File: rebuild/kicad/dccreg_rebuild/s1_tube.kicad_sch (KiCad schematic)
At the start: 11 parts

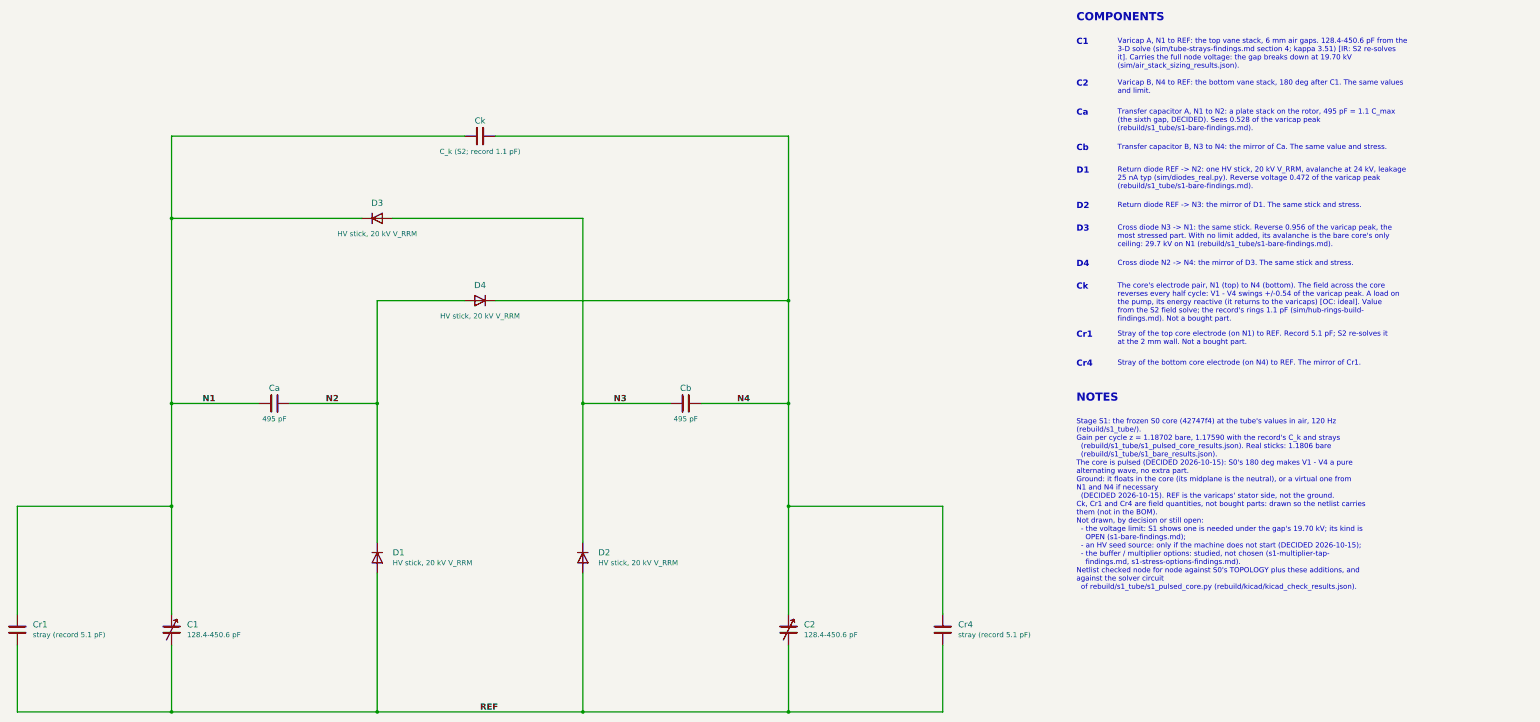
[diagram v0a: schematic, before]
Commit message: feat(rebuild): one KiCad project with a sheet per stage
The designer asked for all stages and changes in one project, each on
its own sheet. rebuild/kicad/dccreg_rebuild/ replaces the two separate
projects: a root sheet indexes the stages, with S0 and S1 as sheets 2
and 3. Each stage numbers its parts in its own hundred (S0 1xx, S1 2xx),
and the nets stay local to their sheet. The layout the designer accepted
is unchanged.

The check exports the project netlist, cuts it by sheet and compares each
stage with its source: S0 against TOPOLOGY and s0_base.cir, S1 against
TOPOLOGY plus the additions and the pulsed-core solver. All match, and
the ERC is clean. A new stage is one entry in STAGES.

Co-Authored-By: Claude Opus 5.5 <noreply@anthropic.com>
Claude-Session: https://claude.ai/code/session_01EZwGpTFL1hyaEya41kJtBw
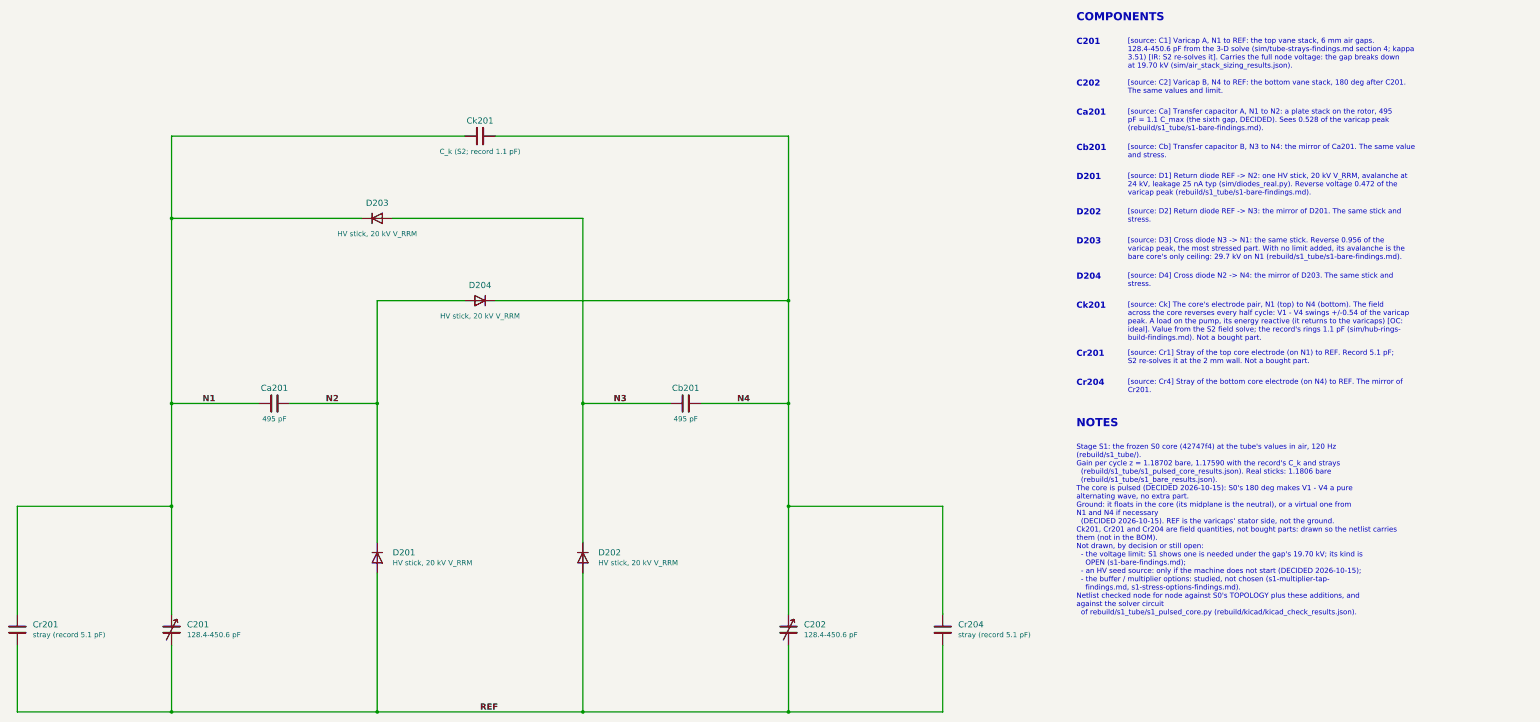
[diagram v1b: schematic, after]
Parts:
- renumbered C1 to C201, C2 to C202, Ca to Ca201, Cb to Cb201, Ck to Ck201, Cr1 to Cr201, Cr4 to Cr204, D1 to D201, D2 to D202, D3 to D203, D4 to D204
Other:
- note added: "C201"
- note added: "C202"
- note added: "Ca201"
- note added: "Cb201"
- note added: "Ck201"
- note added: "Cr201"
- note added: "Cr204"
- note added: "D201"
- note added: "D202"
- note added: "D203"
- note added: "D204"
- note added: "[source: C1] Varicap A, N1 to REF: the top vane stack, 6 mm air gaps. 128.4-450.6 pF from the 3-D solve (sim/tube-strays-findings.md section 4; kappa 3.51) [IR: S2 re-solves it]. Carries the full node voltage: the gap breaks down at 19.70 kV (sim/air_stack_sizing_results.json)."
- note added: "[source: C2] Varicap B, N4 to REF: the bottom vane stack, 180 deg after C201. The same values and limit."
- note added: "[source: Ca] Transfer capacitor A, N1 to N2: a plate stack on the rotor, 495 pF = 1.1 C_max (the sixth gap, DECIDED). Sees 0.528 of the varicap peak (rebuild/s1_tube/s1-bare-findings.md)."
- note added: "[source: Cb] Transfer capacitor B, N3 to N4: the mirror of Ca201. The same value and stress."
- note added: "[source: Ck] The core's electrode pair, N1 (top) to N4 (bottom). The field across the core reverses every half cycle: V1 - V4 swings +/-0.54 of the varicap peak. A load on the pump, its energy reactive (it returns to the varicaps) [OC: ideal]. Value from the S2 field solve; the record's rings 1.1 pF (sim/hub-rings- build-findings.md). Not a bought part."
- note added: "[source: Cr1] Stray of the top core electrode (on N1) to REF. Record 5.1 pF; S2 re-solves it at the 2 mm wall. Not a bought part."
- note added: "[source: Cr4] Stray of the bottom core electrode (on N4) to REF. The mirror of Cr201."
- note added: "[source: D1] Return diode REF -> N2: one HV stick, 20 kV V_RRM, avalanche at 24 kV, leakage 25 nA typ (sim/diodes_real.py). Reverse voltage 0.472 of the varicap peak (rebuild/s1_tube/s1-bare-findings.md)."
- note added: "[source: D2] Return diode REF -> N3: the mirror of D201. The same stick and stress."
- note added: "[source: D3] Cross diode N3 -> N1: the same stick. Reverse 0.956 of the varicap peak, the most stressed part. With no limit added, its avalanche is the bare core's only ceiling: 29.7 kV on N1 (rebuild/s1_tube/s1-bare-findings.md)."
- note added: "[source: D4] Cross diode N2 -> N4: the mirror of D203. The same stick and stress."
- note removed: "C1"
- note removed: "C2"
- note removed: "Ca"
- note removed: "Cb"
- note removed: "Ck"
- note removed: "Cr1"
- note removed: "Cr4"
- note removed: "Cross diode N2 -> N4: the mirror of D3. The same stick and stress."
- note removed: "Cross diode N3 -> N1: the same stick. Reverse 0.956 of the varicap peak, the most stressed part. With no limit added, its avalanche is the bare core's only ceiling: 29.7 kV on N1 (rebuild/s1_tube/s1-bare-findings.md)."
- note removed: "D1"
- note removed: "D2"
- note removed: "D3"
- note removed: "D4"
- note removed: "Return diode REF -> N2: one HV stick, 20 kV V_RRM, avalanche at 24 kV, leakage 25 nA typ (sim/diodes_real.py). Reverse voltage 0.472 of the varicap peak (rebuild/s1_tube/s1-bare-findings.md)."
- note removed: "Return diode REF -> N3: the mirror of D1. The same stick and stress."
- note removed: "Stray of the bottom core electrode (on N4) to REF. The mirror of Cr1."
- note removed: "Stray of the top core electrode (on N1) to REF. Record 5.1 pF; S2 re-solves it at the 2 mm wall. Not a bought part."
- note removed: "The core's electrode pair, N1 (top) to N4 (bottom). The field across the core reverses every half cycle: V1 - V4 swings +/-0.54 of the varicap peak. A load on the pump, its energy reactive (it returns to the varicaps) [OC: ideal]. Value from the S2 field solve; the record's rings 1.1 pF (sim/hub-rings-build- findings.md). Not a bought part."
- note removed: "Transfer capacitor A, N1 to N2: a plate stack on the rotor, 495 pF = 1.1 C_max (the sixth gap, DECIDED). Sees 0.528 of the varicap peak (rebuild/s1_tube/s1-bare-findings.md)."
- note removed: "Transfer capacitor B, N3 to N4: the mirror of Ca. The same value and stress."
- note removed: "Varicap A, N1 to REF: the top vane stack, 6 mm air gaps. 128.4-450.6 pF from the 3-D solve (sim/tube-strays-findings.md section 4; kappa 3.51) [IR: S2 re-solves it]. Carries the full node voltage: the gap breaks down at 19.70 kV (sim/air_stack_sizing_results.json)."
- note removed: "Varicap B, N4 to REF: the bottom vane stack, 180 deg after C1. The same values and limit."

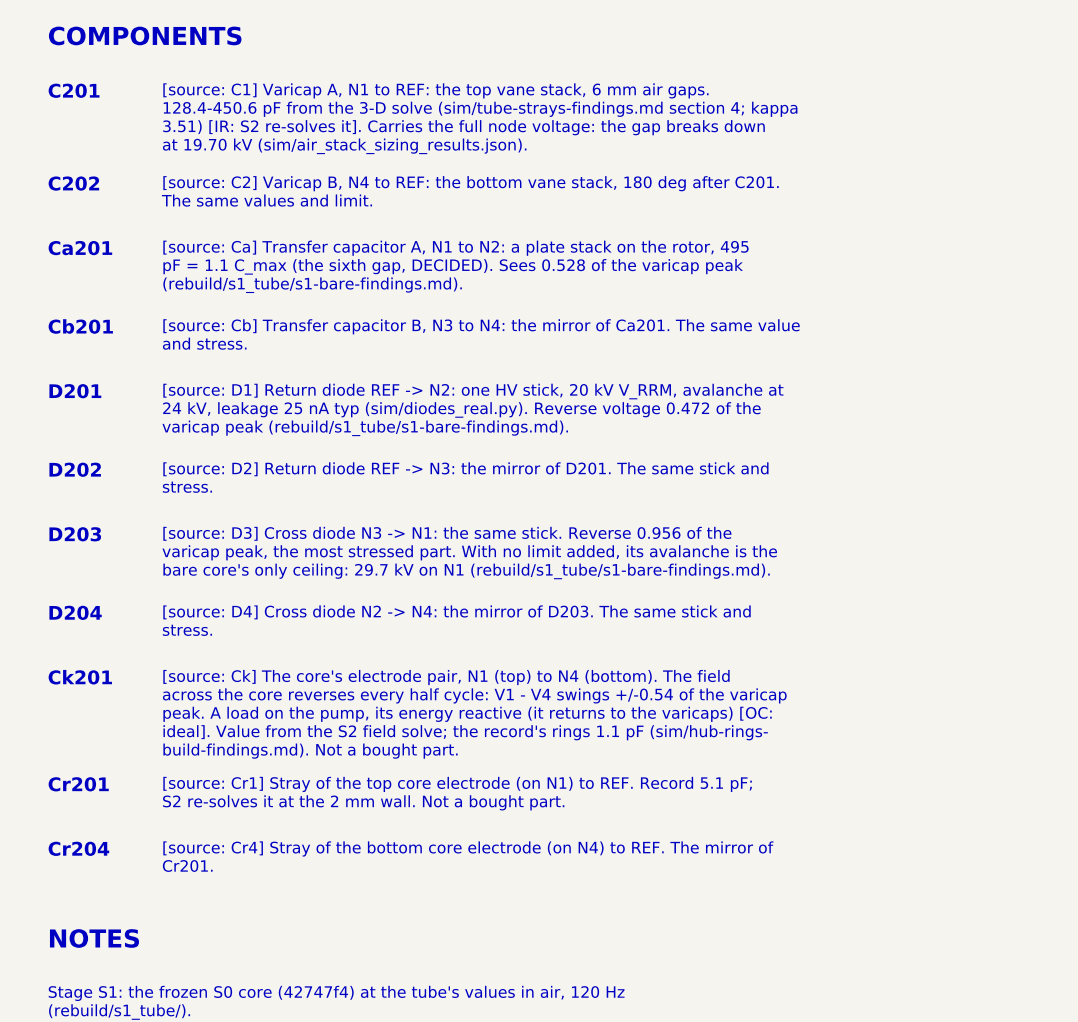
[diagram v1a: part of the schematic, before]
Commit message: feat(rebuild): S2 begins, the plan and the compact deck
The designer's starting choices for S2 (the 3-D models): the 10-11
redesign layout stripped back to the S1b circuit, N1 on side A below the
hub as the record, a rim variant to win back kappa, and the repo's
finite-volume field solver. FreeCAD 1.1.4 is installed beside KiCad.
rebuild/s2_models/s2-plan.md sets out S2a-S2d.

rebuild/s2_models/s2_deck.py plans the deck for the S1b parts only (the
designer: "a bigger deck then required would insert an unnecessary
compromise"), on the redesign study's rules:
- every HV part also clears the grounded can in air (the designer's
  choice): deck r 50-125 against the redesign's r 50-150;
- each clamp string split into two series halves placed against the
  sticks, so the deck balances to 9 g, where a chain plan needed 388 g;
- the column 13 mm off the deck instead of 39, so each side is 26 mm
  shorter;
- the cross wires run straight across, held at the midplane by a PTFE
  bracket with two ribs (41.9 mm creepage against 31.6 needed), as the
  designer asked for now.

Also corrected: N1 is side A (below the hub) in the S1 texts, the S1b
study (re-run, results unchanged) and the KiCad legends (regenerated;
netlists still match, ERC 0/0).

Co-Authored-By: Claude Opus 5.5 <noreply@anthropic.com>
Claude-Session: https://claude.ai/code/session_01EZwGpTFL1hyaEya41kJtBw
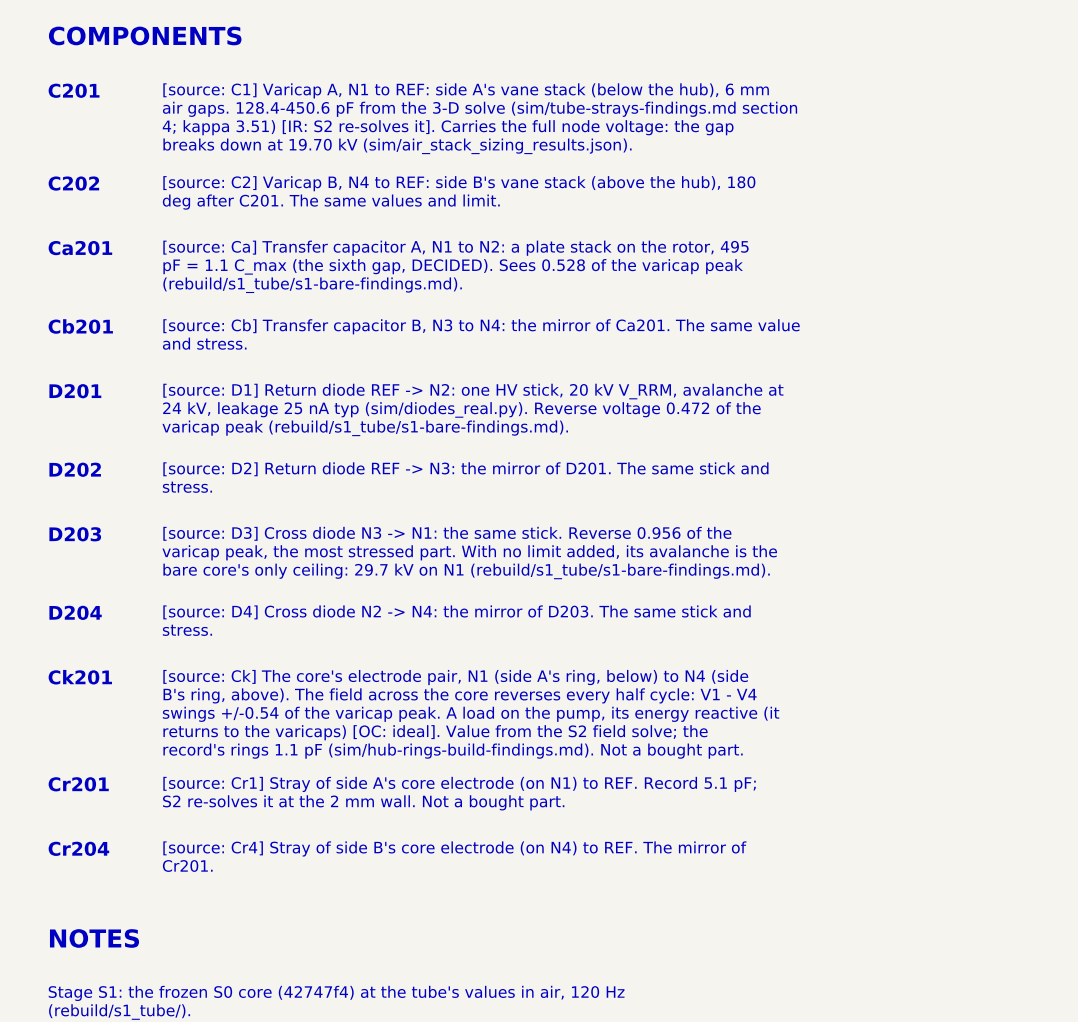
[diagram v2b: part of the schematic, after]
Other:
- note added: "[source: C1] Varicap A, N1 to REF: side A's vane stack (below the hub), 6 mm air gaps. 128.4-450.6 pF from the 3-D solve (sim/tube-strays-findings.md section 4; kappa 3.51) [IR: S2 re-solves it]. Carries the full node voltage: the gap breaks down at 19.70 kV (sim/air_stack_sizing_results.json)."
- note added: "[source: C2] Varicap B, N4 to REF: side B's vane stack (above the hub), 180 deg after C201. The same values and limit."
- note added: "[source: Ck] The core's electrode pair, N1 (side A's ring, below) to N4 (side B's ring, above). The field across the core reverses every half cycle: V1 - V4 swings +/-0.54 of the varicap peak. A load on the pump, its energy reactive (it returns to the varicaps) [OC: ideal]. Value from the S2 field solve; the record's rings 1.1 pF (sim/hub-rings-build-findings.md). Not a bought part."
- note added: "[source: Cr1] Stray of side A's core electrode (on N1) to REF. Record 5.1 pF; S2 re-solves it at the 2 mm wall. Not a bought part."
- note added: "[source: Cr4] Stray of side B's core electrode (on N4) to REF. The mirror of Cr201."
- note removed: "[source: C1] Varicap A, N1 to REF: the top vane stack, 6 mm air gaps. 128.4-450.6 pF from the 3-D solve (sim/tube-strays-findings.md section 4; kappa 3.51) [IR: S2 re-solves it]. Carries the full node voltage: the gap breaks down at 19.70 kV (sim/air_stack_sizing_results.json)."
- note removed: "[source: C2] Varicap B, N4 to REF: the bottom vane stack, 180 deg after C201. The same values and limit."
- note removed: "[source: Ck] The core's electrode pair, N1 (top) to N4 (bottom). The field across the core reverses every half cycle: V1 - V4 swings +/-0.54 of the varicap peak. A load on the pump, its energy reactive (it returns to the varicaps) [OC: ideal]. Value from the S2 field solve; the record's rings 1.1 pF (sim/hub-rings- build-findings.md). Not a bought part."
- note removed: "[source: Cr1] Stray of the top core electrode (on N1) to REF. Record 5.1 pF; S2 re-solves it at the 2 mm wall. Not a bought part."
- note removed: "[source: Cr4] Stray of the bottom core electrode (on N4) to REF. The mirror of Cr201."
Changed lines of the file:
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@@
 		)
 	)
-	(text "[source: C1] Varicap A, N1 to REF: the top vane stack, 6 mm air gaps.\n128.4-450.6 pF from the 3-D solve (sim/tube-strays-findings.md section 4; kappa\n3.51) [IR: S2 re-solves it]. Carries the full node voltage: the gap breaks down\nat 19.70 kV (sim/air_stack_sizing_results.json)."
+	(text "[source: C1] Varicap A, N1 to REF: side A's vane stack (below the hub), 6 mm\nair gaps. 128.4-450.6 pF from the 3-D solve (sim/tube-strays-findings.md section\n4; kappa 3.51) [IR: S2 re-solves it]. Carries the full node voltage: the gap\nbreaks down at 19.70 kV (sim/air_stack_sizing_results.json)."
 		(exclude_from_sim yes)
 		(at 307.34 21.59 0)
@@
 		)
 	)
-	(text "[source: C2] Varicap B, N4 to REF: the bottom vane stack, 180 deg after C201.\nThe same values and limit."
+	(text "[source: C2] Varicap B, N4 to REF: side B's vane stack (above the hub), 180\ndeg after C201. The same values and limit."
 		(exclude_from_sim yes)
 		(at 307.34 31.90 0)
@@
 		)
 	)
-	(text "[source: Ck] The core's electrode pair, N1 (top) to N4 (bottom). The field\nacross the core reverses every half cycle: V1 - V4 swings +/-0.54 of the varicap\npeak. A load on the pump, its energy reactive (it returns to the varicaps) [OC:\nideal]. Value from the S2 field solve; the record's rings 1.1 pF (sim/hub-rings-\nbuild-findings.md). Not a bought part."
+	(text "[source: Ck] The core's electrode pair, N1 (side A's ring, below) to N4 (side\nB's ring, above). The field across the core reverses every half cycle: V1 - V4\nswings +/-0.54 of the varicap peak. A load on the pump, its energy reactive (it\nreturns to the varicaps) [OC: ideal]. Value from the S2 field solve; the\nrecord's rings 1.1 pF (sim/hub-rings-build-findings.md). Not a bought part."
 		(exclude_from_sim yes)
 		(at 307.34 86.77 0)
@@
 		)
 	)
-	(text "[source: Cr1] Stray of the top core electrode (on N1) to REF. Record 5.1 pF;\nS2 re-solves it at the 2 mm wall. Not a bought part."
+	(text "[source: Cr1] Stray of side A's core electrode (on N1) to REF. Record 5.1 pF;\nS2 re-solves it at the 2 mm wall. Not a bought part."
 		(exclude_from_sim yes)
 		(at 307.34 98.65 0)
@@
 		)
 	)
-	(text "[source: Cr4] Stray of the bottom core electrode (on N4) to REF. The mirror of\nCr201."
+	(text "[source: Cr4] Stray of side B's core electrode (on N4) to REF. The mirror of\nCr201."
 		(exclude_from_sim yes)
 		(at 307.34 105.82 0)
@@
 			)
 		)
-		(property "Description" "Varicap A, N1 to REF: the top vane stack, 6 mm air gaps. 128.4-450.6 pF from the 3-D solve (sim/tube-strays-findings.md section 4; kappa 3.51) [IR: S2 re-solves it]. Carries the full node voltage: the gap breaks down at 19.70 kV (sim/air_stack_sizing_results.json)."
+		(property "Description" "Varicap A, N1 to REF: side A's vane stack (below the hub), 6 mm air gaps. 128.4-450.6 pF from the 3-D solve (sim/tube-strays-findings.md section 4; kappa 3.51) [IR: S2 re-solves it]. Carries the full node voltage: the gap breaks down at 19.70 kV (sim/air_stack_sizing_results.json)."
 			(at 71.12 167.64 0)
 			(hide yes)
@@
 			)
 		)
-		(property "Description" "Varicap B, N4 to REF: the bottom vane stack, 180 deg after C201. The same values and limit."
+		(property "Description" "Varicap B, N4 to REF: side B's vane stack (above the hub), 180 deg after C201. The same values and limit."
 			(at 223.52 167.64 0)
 			(hide yes)
@@
 			)
 		)
-		(property "Description" "The core's electrode pair, N1 (top) to N4 (bottom). The field across the core reverses every half cycle: V1 - V4 swings +/-0.54 of the varicap peak. A load on the pump, its energy reactive (it returns to the varicaps) [OC: ideal]. Value from the S2 field solve; the record's rings 1.1 pF (sim/hub-rings-build-findings.md). Not a bought part."
+		(property "Description" "The core's electrode pair, N1 (side A's ring, below) to N4 (side B's ring, above). The field across the core reverses every half cycle: V1 - V4 swings +/-0.54 of the varicap peak. A load on the pump, its energy reactive (it returns to the varicaps) [OC: ideal]. Value from the S2 field solve; the record's rings 1.1 pF (sim/hub-rings-build-findings.md). Not a bought part."
 			(at 147.32 45.72 90)
 			(hide yes)
@@
 			)
 		)
-		(property "Description" "Stray of the top core electrode (on N1) to REF. Record 5.1 pF; S2 re-solves it at the 2 mm wall. Not a bought part."
+		(property "Description" "Stray of side A's core electrode (on N1) to REF. Record 5.1 pF; S2 re-solves it at the 2 mm wall. Not a bought part."
 			(at 33.02 167.64 0)
 			(hide yes)
@@
 			)
 		)
-		(property "Description" "Stray of the bottom core electrode (on N4) to REF. The mirror of Cr201."
+		(property "Description" "Stray of side B's core electrode (on N4) to REF. The mirror of Cr201."
 			(at 261.62 167.64 0)
 			(hide yes)
